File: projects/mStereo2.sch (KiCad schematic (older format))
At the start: 18 parts, among them P101 CONN_AMANERO, P102 MOLEX KK 1x2, P103 MOLEX KK 1X3, P104 NC3MAHL, P105 NC3MAHL, U101 ISO7640, U102 CDCLVC1104, U103 MCP100-315DI, U104 SRC4192, X101 XTAL

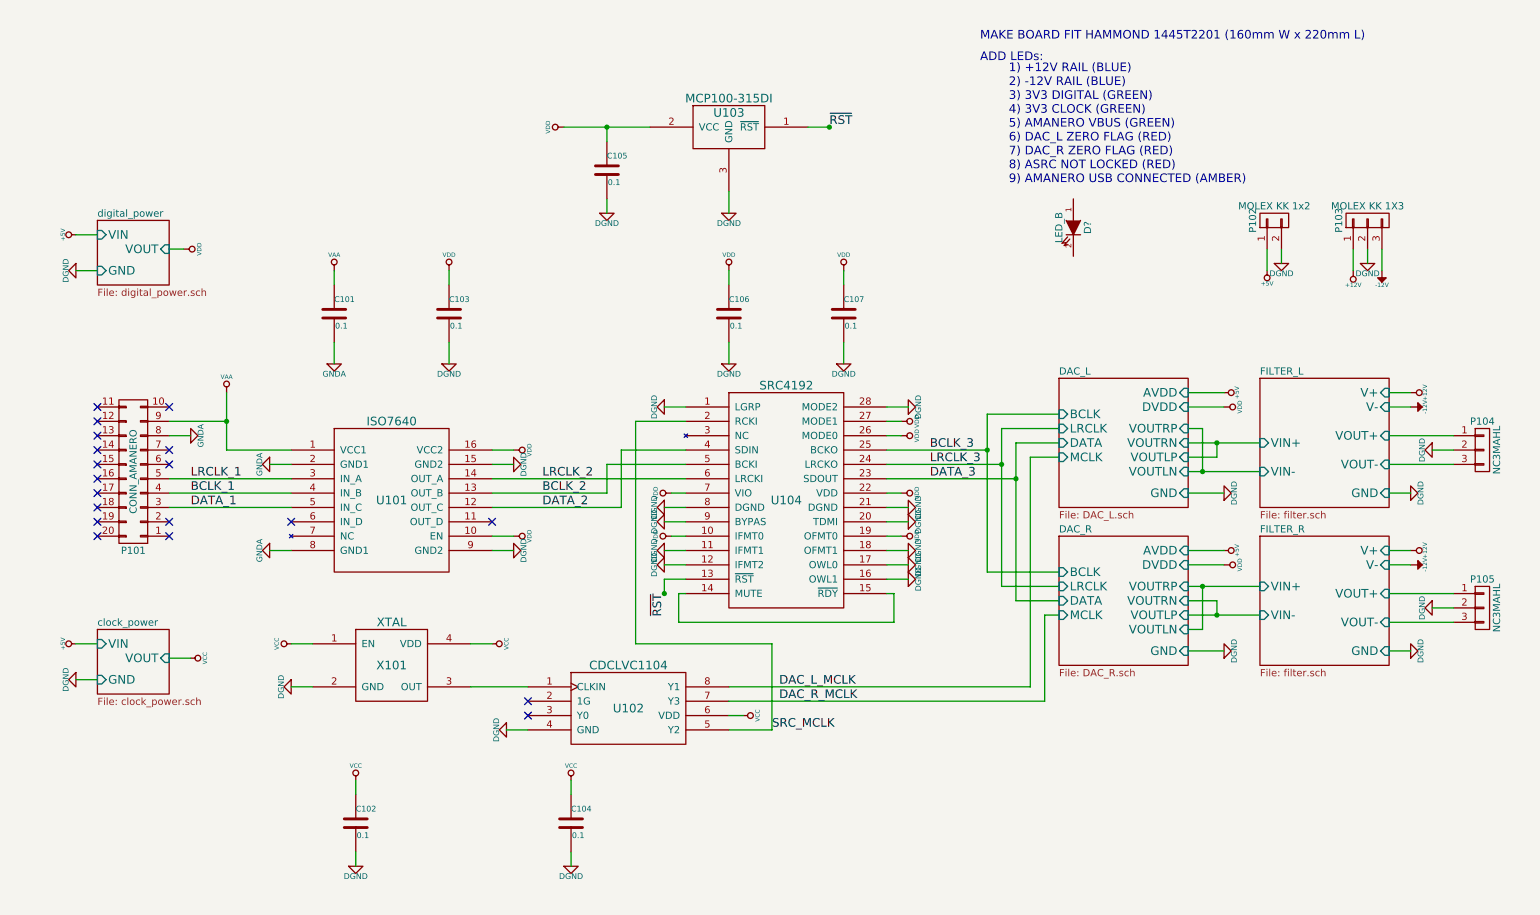
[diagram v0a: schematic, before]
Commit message: updated LED indicators in schematic files (*.sch)
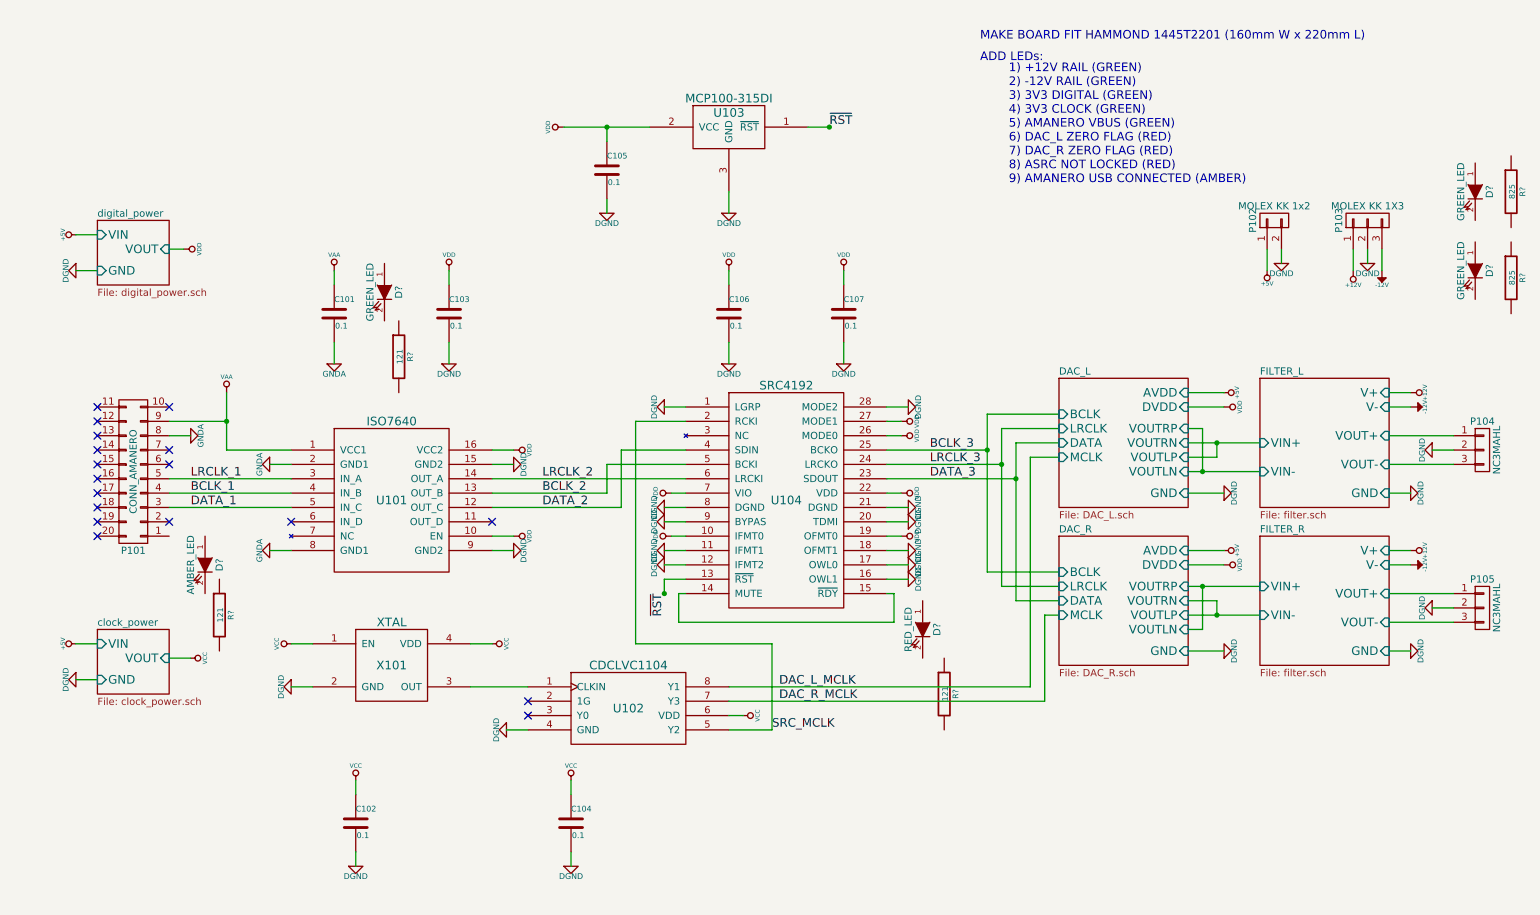
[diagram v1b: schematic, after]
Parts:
- removed D?: LED_B, symbol LED
- added D? (x3): GREEN_LED, symbol GREEN_LED
- added D?: AMBER_LED, symbol AMBER_LED
- added D?: RED_LED, symbol RED_LED
- added R? (x3): 121, symbol R
- added R? (x2): 825, symbol R
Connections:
- no-connect marks 19 -> 18
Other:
- note added: "1) +12V RAIL (GREEN)\n2) -12V RAIL (GREEN)\n3) 3V3 DIGITAL (GREEN)\n4) 3V3 CLOCK (GREEN)\n5) AMANERO VBUS (GREEN)\n6) DAC_L ZERO FLAG (RED)\n7) DAC_R ZERO FLAG (RED)\n8) ASRC NOT LOCKED (RED)\n9) AMANERO USB CONNECTED (AMBER)\n"
- note removed: "1) +12V RAIL (BLUE)\n2) -12V RAIL (BLUE)\n3) 3V3 DIGITAL (GREEN)\n4) 3V3 CLOCK (GREEN)\n5) AMANERO VBUS (GREEN)\n6) DAC_L ZERO FLAG (RED)\n7) DAC_R ZERO FLAG (RED)\n8) ASRC NOT LOCKED (RED)\n9) AMANERO USB CONNECTED (AMBER)\n"
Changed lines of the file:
@@
 LIBS:microchip_gosselin
 LIBS:linear_technology_gosselin
+LIBS:led_gosselin
 LIBS:mStereo2-cache
 EELAYER 24 0
@@
 $EndComp
 NoConn ~ 1150 4200
-NoConn ~ 1650 4200
 NoConn ~ 1650 3300
 NoConn ~ 1650 3700
@@
 ADD LEDs:
 Text Notes 7500 1750 0    60   ~ 0
-1) +12V RAIL (BLUE)\n2) -12V RAIL (BLUE)\n3) 3V3 DIGITAL (GREEN)\n4) 3V3 CLOCK (GREEN)\n5) AMANERO VBUS (GREEN)\n6) DAC_L ZERO FLAG (RED)\n7) DAC_R ZERO FLAG (RED)\n8) ASRC NOT LOCKED (RED)\n9) AMANERO USB CONNECTED (AMBER)\n
-$Comp
-L LED D?
-U 1 1 544F542B
-P 7950 2050
-F 0 "D?" H 7950 2150 50  0000 C CNN
-F 1 "LED_B" H 7950 1950 50  0000 C CNN
-F 2 "" H 7950 2050 60  0000 C CNN
-F 3 "" H 7950 2050 60  0000 C CNN
-	1    7950 2050
-	0    1    1    0
+1) +12V RAIL (GREEN)\n2) -12V RAIL (GREEN)\n3) 3V3 DIGITAL (GREEN)\n4) 3V3 CLOCK (GREEN)\n5) AMANERO VBUS (GREEN)\n6) DAC_L ZERO FLAG (RED)\n7) DAC_R ZERO FLAG (RED)\n8) ASRC NOT LOCKED (RED)\n9) AMANERO USB CONNECTED (AMBER)\n
+$Comp
+L GREEN_LED D?
+U 1 1 5454BA40
+P 10750 1800
+F 0 "D?" H 10750 1900 50  0000 C CNN
+F 1 "GREEN_LED" H 10750 1700 50  0000 C CNN
+F 2 "" H 10750 1800 60  0000 C CNN
+F 3 "" H 10750 1800 60  0000 C CNN
+F 4 " 160-1423-1-ND" H 10950 2100 60  0001 C CNN "Supplier-PN"
+F 5 "Digi-key" H 10850 2000 60  0001 C CNN "Supplier"
+F 6 "LED GREEN CLEAR THIN 0805 SMD" H 11250 2400 60  0001 C CNN "Description"
+F 7 "Lite-On" H 11050 2200 60  0001 C CNN "Manu"
+F 8 "LTST-C171GKT" H 11150 2300 60  0001 C CNN "Manu-PN"
+	1    10750 1800
+	0    1    1    0
+$EndComp
+$Comp
+L GREEN_LED D?
+U 1 1 5454BB10
+P 10750 2350
+F 0 "D?" H 10750 2450 50  0000 C CNN
+F 1 "GREEN_LED" H 10750 2250 50  0000 C CNN
+F 2 "" H 10750 2350 60  0000 C CNN
+F 3 "" H 10750 2350 60  0000 C CNN
+F 4 " 160-1423-1-ND" H 10950 2650 60  0001 C CNN "Supplier-PN"
+F 5 "Digi-key" H 10850 2550 60  0001 C CNN "Supplier"
+F 6 "LED GREEN CLEAR THIN 0805 SMD" H 11250 2950 60  0001 C CNN "Description"
+F 7 "Lite-On" H 11050 2750 60  0001 C CNN "Manu"
+F 8 "LTST-C171GKT" H 11150 2850 60  0001 C CNN "Manu-PN"
+	1    10750 2350
+	0    1    1    0
+$EndComp
+$Comp
+L GREEN_LED D?
+U 1 1 5454DE9D
+P 3150 2500
+F 0 "D?" H 3150 2600 50  0000 C CNN
+F 1 "GREEN_LED" H 3150 2400 50  0000 C CNN
+F 2 "" H 3150 2500 60  0000 C CNN
+F 3 "" H 3150 2500 60  0000 C CNN
+F 4 " 160-1423-1-ND" H 3350 2800 60  0001 C CNN "Supplier-PN"
+F 5 "Digi-key" H 3250 2700 60  0001 C CNN "Supplier"
+F 6 "LED GREEN CLEAR THIN 0805 SMD" H 3650 3100 60  0001 C CNN "Description"
+F 7 "Lite-On" H 3450 2900 60  0001 C CNN "Manu"
+F 8 "LTST-C171GKT" H 3550 3000 60  0001 C CNN "Manu-PN"
+	1    3150 2500
+	0    1    1    0
+$EndComp
+$Comp
+L R R?
+U 1 1 5454DFE8
+P 3250 2950
+F 0 "R?" V 3330 2950 40  0000 C CNN
+F 1 "121" V 3257 2951 40  0000 C CNN
+F 2 "" V 3180 2950 30  0000 C CNN
+F 3 "" H 3250 2950 30  0000 C CNN
+F 4 "Digi-key" H 3250 2950 60  0001 C CNN "Supplier"
+F 5 "RNCP0805FTD121RCT-ND" H 3250 2950 60  0001 C CNN "Supplier-PN"
+F 6 "Stackpole" H 3250 2950 60  0001 C CNN "Manu"
+F 7 "RNCP0805FTD121R" H 3250 2950 60  0001 C CNN "Manu-PN"
+F 8 "RES 121 OHM 1/4W 1% 0805" H 3250 2950 60  0001 C CNN "Description"
+	1    3250 2950
+	1    0    0    -1
+$EndComp
+$Comp
+L R R?
+U 1 1 54554A5A
+P 11000 1800
+F 0 "R?" V 11080 1800 40  0000 C CNN
+F 1 "825" V 11007 1801 40  0000 C CNN
+F 2 "" V 10930 1800 30  0000 C CNN
+F 3 "" H 11000 1800 30  0000 C CNN
+F 4 "Digi-key" H 11000 1800 60  0001 C CNN "Supplier"
+F 5 "RNCP0805FTD825RCT-ND" H 11000 1800 60  0001 C CNN "Supplier-PN"
+F 6 "Stackpole" H 11000 1800 60  0001 C CNN "Manu"
+F 7 "RNCP0805FTD825R" H 11000 1800 60  0001 C CNN "Manu-PN"
+F 8 "RES 825 OHM 1/4W 1% 0805" H 11000 1800 60  0001 C CNN "Description"
+	1    11000 1800
+	1    0    0    -1
+$EndComp
+$Comp
+L R R?
+U 1 1 545557E1
+P 11000 2400
+F 0 "R?" V 11080 2400 40  0000 C CNN
+F 1 "825" V 11007 2401 40  0000 C CNN
+F 2 "" V 10930 2400 30  0000 C CNN
+F 3 "" H 11000 2400 30  0000 C CNN
+F 4 "Digi-key" H 11000 2400 60  0001 C CNN "Supplier"
+F 5 "RNCP0805FTD825RCT-ND" H 11000 2400 60  0001 C CNN "Supplier-PN"
+F 6 "Stackpole" H 11000 2400 60  0001 C CNN "Manu"
+F 7 "RNCP0805FTD825R" H 11000 2400 60  0001 C CNN "Manu-PN"
+F 8 "RES 825 OHM 1/4W 1% 0805" H 11000 2400 60  0001 C CNN "Description"
+	1    11000 2400
+	1    0    0    -1
+$EndComp
+$Comp
+L AMBER_LED D?
+U 1 1 5455668B
+P 1900 4400
+F 0 "D?" H 1900 4500 50  0000 C CNN
+F 1 "AMBER_LED" H 1900 4300 50  0000 C CNN
+F 2 "" H 1900 4400 60  0000 C CNN
+F 3 "" H 1900 4400 60  0000 C CNN
+F 4 "492-1695-1-ND" H 2100 4700 60  0001 C CNN "Supplier-PN"
+F 5 "Bivar" H 2200 4800 60  0001 C CNN "Manu"
+F 6 "Digi-key" H 2000 4600 60  0001 C CNN "Supplier"
+F 7 "LED AMBER 610NM WATER CLEAR 0805" H 2400 5000 60  0001 C CNN "Description"
+F 8 "SM0805AC" H 2300 4900 60  0001 C CNN "Manu-PN"
+	1    1900 4400
+	0    1    1    0
+$EndComp
+$Comp
+L R R?
+U 1 1 54556747
+P 2000 4750
+F 0 "R?" V 2080 4750 40  0000 C CNN
+F 1 "121" V 2007 4751 40  0000 C CNN
+F 2 "" V 1930 4750 30  0000 C CNN
+F 3 "" H 2000 4750 30  0000 C CNN
+F 4 "Digi-key" H 2000 4750 60  0001 C CNN "Supplier"
+F 5 "RNCP0805FTD121RCT-ND" H 2000 4750 60  0001 C CNN "Supplier-PN"
+F 6 "Stackpole" H 2000 4750 60  0001 C CNN "Manu"
+F 7 "RNCP0805FTD121R" H 2000 4750 60  0001 C CNN "Manu-PN"
+F 8 "RES 121 OHM 1/4W 1% 0805" H 2000 4750 60  0001 C CNN "Description"
+	1    2000 4750
+	1    0    0    -1
+$EndComp
+$Comp
+L RED_LED D?
+U 1 1 5455968D
+P 6900 4850
+F 0 "D?" H 6900 4950 50  0000 C CNN
+F 1 "RED_LED" H 6900 4750 50  0000 C CNN
+F 2 "" H 6900 4850 60  0000 C CNN
+F 3 "" H 6900 4850 60  0000 C CNN
+F 4 "160-1427-1-ND" H 7100 5150 60  0001 C CNN "Supplier-PN"
+F 5 "Digi-key" H 7000 5050 60  0001 C CNN "Supplier"
+F 6 "LED SUPER RED CLR THIN 0805 SMD" H 7400 5450 60  0001 C CNN "Description"
+F 7 "Lite-On" H 7200 5250 60  0001 C CNN "Manu"
+F 8 "LTST-C171KRKT" H 7300 5350 60  0001 C CNN "Manu-PN"
+	1    6900 4850
+	0    1    1    0
+$EndComp
+$Comp
+L R R?
+U 1 1 5455B453
+P 7050 5300
+F 0 "R?" V 7130 5300 40  0000 C CNN
+F 1 "121" V 7057 5301 40  0000 C CNN
+F 2 "" V 6980 5300 30  0000 C CNN
+F 3 "" H 7050 5300 30  0000 C CNN
+F 4 "Digi-key" H 7050 5300 60  0001 C CNN "Supplier"
+F 5 "RNCP0805FTD121RCT-ND" H 7050 5300 60  0001 C CNN "Supplier-PN"
+F 6 "Stackpole" H 7050 5300 60  0001 C CNN "Manu"
+F 7 "RNCP0805FTD121R" H 7050 5300 60  0001 C CNN "Manu-PN"
+F 8 "RES 121 OHM 1/4W 1% 0805" H 7050 5300 60  0001 C CNN "Description"
+	1    7050 5300
+	1    0    0    -1
 $EndComp
 $EndSCHEMATC

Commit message: updated LEDs in schematic, output connectors, re-annotated
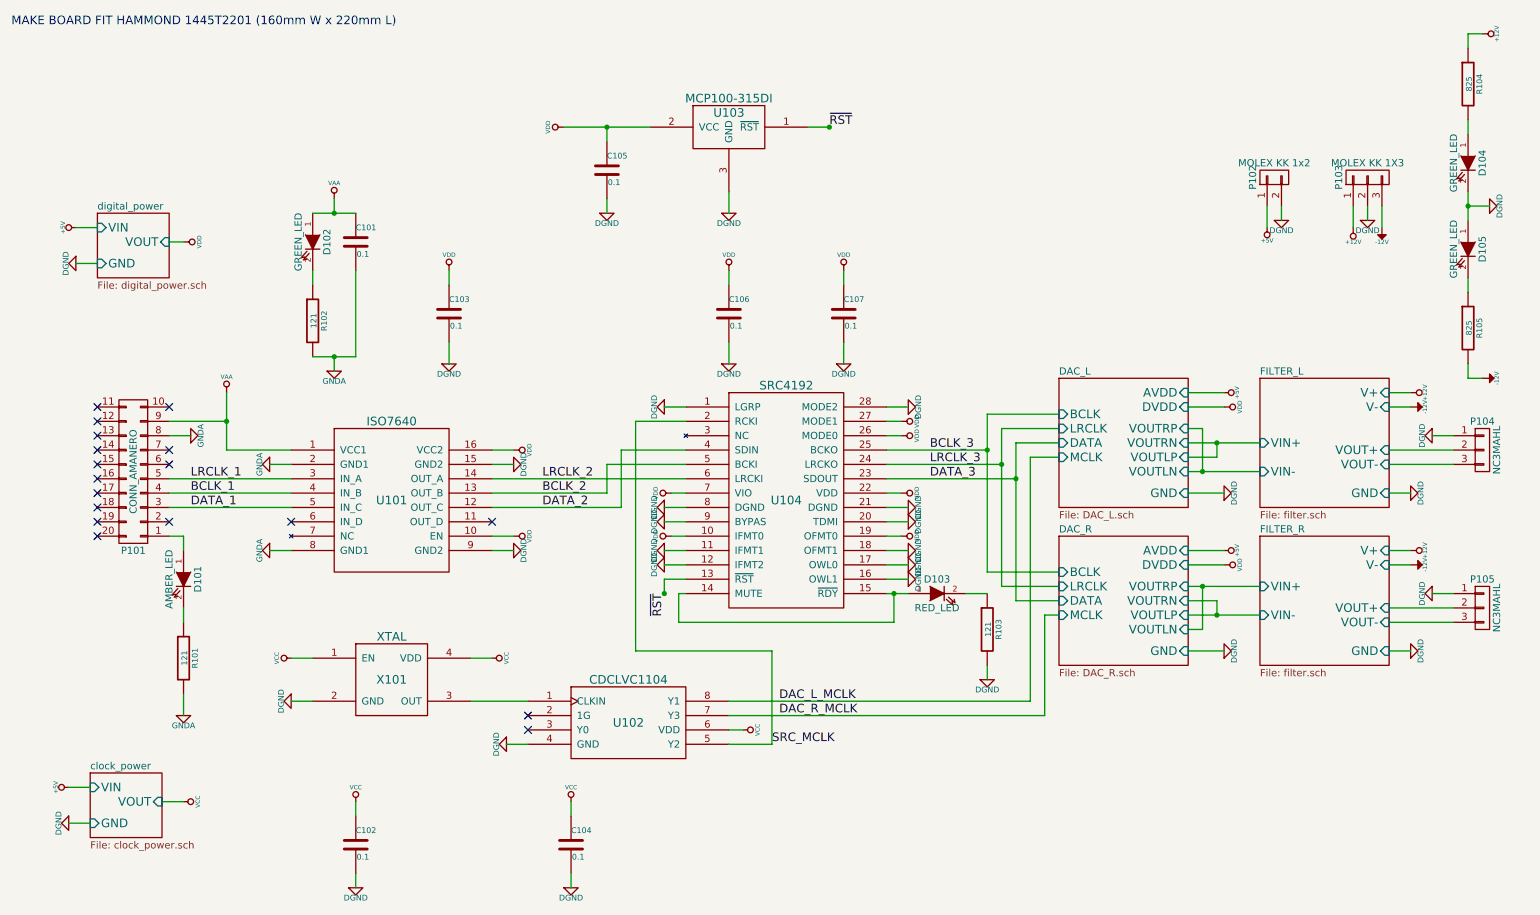
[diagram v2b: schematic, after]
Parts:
- gave numbers to parts that had none: 10
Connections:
- net +12V: now also R104.1
- net -12V: now also R105.2
- net DGND: now also D104.2 (K), D105.1 (A), P104.1 (P1), P105.1 (P1), R103.2; no longer P104.2 (P2), P105.2 (P2)
- net FILTER_L/VOUT+: now also P104.2 (P2); no longer P104.1 (P1)
- net FILTER_R/VOUT+: now also P105.2 (P2); no longer P105.1 (P1)
- net GNDA: now also R101.2, R102.2
- net VAA: now also D102.1 (A)
- net at P101.1 (P1): now also D101.1 (A)
- net at U104.14 (MUTE), U104.15 (~RDY): now also D103.1 (A)
- net at D104.1 (A): now also R104.2
- net at D105.2 (K): now also R105.1
- net at D102.2 (K): now also R102.1
- net at D101.2 (K): now also R101.1
- net at D103.2 (K): now also R103.1
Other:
- note removed: "1) +12V RAIL (GREEN)\n2) -12V RAIL (GREEN)\n3) 3V3 DIGITAL (GREEN)\n4) 3V3 CLOCK (GREEN)\n5) AMANERO VBUS (GREEN)\n6) DAC_L ZERO FLAG (RED)\n7) DAC_R ZERO FLAG (RED)\n8) ASRC NOT LOCKED (RED)\n9) AMANERO USB CONNECTED (AMBER)\n"
- note removed: "ADD LEDs:"
- moved on the sheet: C101, C102, C104, D101, D102, D103, D104, D105, P102, P103, R101, R102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

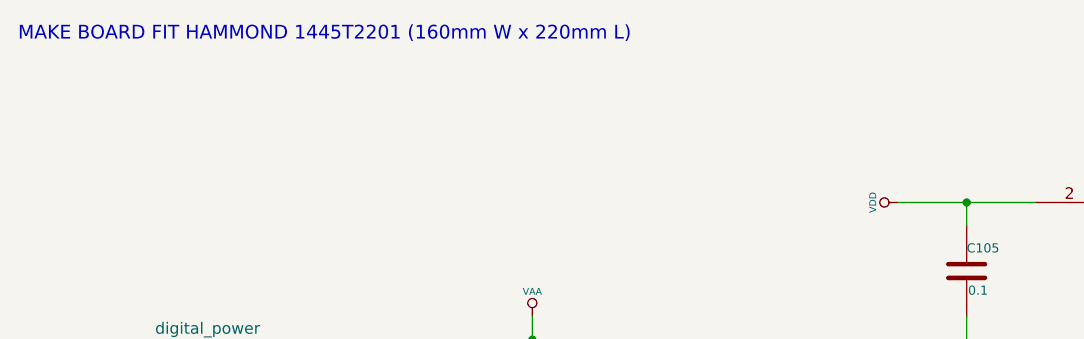
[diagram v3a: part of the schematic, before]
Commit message: updated cvpcb footprint/component links
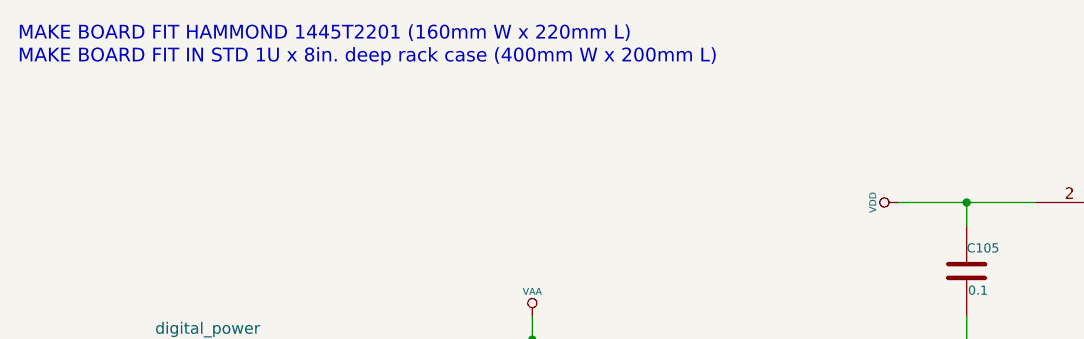
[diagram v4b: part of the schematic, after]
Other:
- note added: "MAKE BOARD FIT IN STD 1U x 8in. deep rack case (400mm W x 200mm L)"
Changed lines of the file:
@@
 Wire Wire Line
 	10450 4600 10600 4600
+Text Notes 550  750  0    60   ~ 0
+MAKE BOARD FIT IN STD 1U x 8in. deep rack case (400mm W x 200mm L)
 $EndSCHEMATC
